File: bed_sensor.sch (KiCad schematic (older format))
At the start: 13 parts, among them J1 Conn_01x02, J2 Conn_01x06, J3 Conn_01x02, J4 Conn_01x08, Q1 2N2219, SW1 SW_SPST

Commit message: add csv
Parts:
- RV1: footprint Potentiometer_THT:Potentiometer_ACP_CA6-H2,5_Horizontal -> Potentiometer_THT:Potentiometer_Piher_PC-16_Single_Vertical
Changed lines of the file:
@@
 EESchema Schematic File Version 4
+LIBS:bed_sensor-cache
 EELAYER 26 0
 EELAYER END
@@
 F 0 "RV1" H 4530 3604 50  0000 R CNN
 F 1 "10K" H 4530 3695 50  0000 R CNN
-F 2 "Potentiometer_THT:Potentiometer_ACP_CA6-H2,5_Horizontal" H 4600 3650 50  0001 C CNN
+F 2 "Potentiometer_THT:Potentiometer_Piher_PC-16_Single_Vertical" H 4600 3650 50  0001 C CNN
 F 3 "~" H 4600 3650 50  0001 C CNN
 	1    4600 3650

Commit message: added CFAH0802d
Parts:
- removed BZ1: Buzzer, Buzzer_Beeper:MagneticBuzzer_Kingstate_KCG0601, symbol Device:Buzzer
- removed D1: D, Diode_THT:D_DO-35_SOD27_P7.62mm_Horizontal, symbol Device:D
- removed DS1: WC1602A, components:NHD-0216HZ-FSW-FBW-33V3C, symbol Display_Character:WC1602A
- removed J1: Conn_01x02, components:JSTPH2, symbol Connector_Generic:Conn_01x02
- removed J2: Conn_01x06, Connector_PinHeader_2.54mm:PinHeader_1x06_P2.54mm_Horizontal, symbol Connector_Generic:Conn_01x06
- removed J3: Conn_01x02, Connector_PinHeader_2.54mm:PinHeader_1x02_P2.54mm_Vertical, symbol Connector_Generic:Conn_01x02
- removed J4: Conn_01x08, Connector_PinSocket_2.54mm:PinSocket_1x08_P2.54mm_Vertical, symbol Connector_Generic:Conn_01x08
- removed Q1: 2N2219, Package_TO_SOT_THT:TO-92_Inline, symbol Transistor_BJT:2N2219
- removed R1: 220, Resistor_THT:R_Axial_DIN0207_L6.3mm_D2.5mm_P7.62mm_Horizontal, symbol Device:R
- removed R2: 1K, Resistor_THT:R_Axial_DIN0207_L6.3mm_D2.5mm_P7.62mm_Horizontal, symbol Device:R
- removed RV1: 10K, Potentiometer_THT:Potentiometer_Piher_PC-16_Single_Vertical, symbol Device:POT
- removed SW1: SW_SPST, Button_Switch_THT:SW_CuK_OS102011MA1QN1_SPDT_Angled, symbol Switch:SW_SPST
- removed uP1: ARDUPROMINI, components:ArduProMini, symbol ardunio_mini:ARDUPROMINI
- added BZ?: Buzzer, symbol Device:Buzzer
- added C? (x2): CP1, symbol Device:CP1
- added C?: C, symbol Device:C
- added D?: LED, symbol Device:LED
- added D?: D, symbol Device:D
- added J?: Conn_01x02, symbol Connector:Conn_01x02
- added Q?: 2N2219, Package_TO_SOT_THT:TO-39-3, symbol Transistor_BJT:2N2219
- added R? (x2): R, symbol Device:R
- added R?: 220, symbol Device:R
- added RV?: POT, symbol device:POT
- added SW?: SW_DPST_x2, symbol foot_sensor-rescue:SW_DPST_x2
- added U?: CFAH0802D-YYH-JP, symbol Crystalfontz:CFAH0802D-YYH-JP
- added U?: SPX3819M5-L-3-3, TO_SOT_Packages_SMD:SOT-23-5, symbol foot_sensor-rescue:SPX3819M5-L-3-3
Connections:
- net labels added: Buzzer, Display_Enable, Vibration
- net labels removed: E, SCL, SDA, buzzer, vib
- wire segments 3 -> 20

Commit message: updated schematic
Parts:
- removed J?: Conn_01x02, symbol Connector:Conn_01x02
- removed RV?: POT, symbol device:POT
- removed SW?: SW_DPST_x2, symbol foot_sensor-rescue:SW_DPST_x2
- removed U?: CFAH0802D-YYH-JP, symbol Crystalfontz:CFAH0802D-YYH-JP
- removed U?: SPX3819M5-L-3-3, TO_SOT_Packages_SMD:SOT-23-5, symbol foot_sensor-rescue:SPX3819M5-L-3-3
- added C2: 10nF, Capacitor_SMD:C_0603_1608Metric, symbol Device:C
- added C5: .1uF, Capacitor_SMD:C_0603_1608Metric, symbol Device:C
- added C6: 1uF, Capacitor_SMD:C_0603_1608Metric, symbol Device:C
- added C7: 10uF, Capacitor_SMD:C_0603_1608Metric, symbol Device:C
- added J1: Conn_01x02, Connector_PinHeader_2.54mm:PinHeader_1x02_P2.54mm_Vertical, symbol Connector_Generic:Conn_01x02
- added J?: Conn_01x02, symbol Connector_Generic:Conn_01x02
- added L1: 10uH, Inductors_SMD:L_Taiyo-Yuden_NR-40xx, symbol Device:L_Core_Ferrite_Small
- added Q2, Q3: BSS138, Package_TO_SOT_SMD:SOT-23, symbol Transistor_FET:BSS138
- added R1, R2, R6, R7: 10k, Resistor_SMD:R_0805_2012Metric, symbol Device:R
- added RV1: 10K, Potentiometers:Potentiometer_Trimmer_ACP_CA9h2.5_Vertical_Px2.5mm_Py5.0mm, symbol Device:R_POT
- added SW1: SW_SPST, components:SW_CuK_OS102011MA1QN1_SPDT_Angled, symbol Switch:SW_SPST
- added U1: MIC5205-3.3, Package_TO_SOT_SMD:SOT-23-5, symbol Regulator_Linear:MIC5205-3.3
- added U2: MPU-9250, Package_DFN_QFN:QFN-24-1EP_3x3mm_P0.4mm_EP1.75x1.6mm, symbol Sensor_Motion:MPU-9250
- added U3: TXB0104D, Package_SO:SOIC-14_3.9x8.7mm_P1.27mm, symbol Logic_LevelTranslator:TXB0104D
- added U4: LTC3525-5, Package_TO_SOT_SMD:SOT-363_SC-70-6, symbol Regulator_Switching:LTC3525-5
- added U5: CFAH0802D-YYH-JP, components:CFAH0802D-YYH-JP, symbol Crystalfontz:CFAH0802D-YYH-JP
- BZ1: renamed from BZ?; footprint (none) -> components:PS1240P02BT
- C1: renamed from C?; value CP1 -> 10uF; footprint (none) -> Capacitors_Tantalum_SMD:CP_Tantalum_Case-T_EIA-3528-12_Reflow
- C3: renamed from C?; value CP1 -> 10uF; footprint (none) -> Capacitors_Tantalum_SMD:CP_Tantalum_Case-B_EIA-3528-21_Reflow
- C4: renamed from C?; value C -> .1uF; footprint (none) -> Capacitor_SMD:C_0603_1608Metric
- D1: renamed from D?; footprint (none) -> LED_SMD:LED_0603_1608Metric
- D2: renamed from D?; footprint (none) -> Diode_SMD:D_0603_1608Metric
- Q1: renamed from Q?; footprint Package_TO_SOT_THT:TO-39-3 -> Package_TO_SOT_SMD:SOT-723
- R3: renamed from R?; value R -> 10k; footprint (none) -> Resistor_SMD:R_0805_2012Metric
- R4: renamed from R?; value R -> 1K; footprint (none) -> Resistor_SMD:R_0805_2012Metric
- R5: renamed from R?; footprint (none) -> Resistor_SMD:R_0805_2012Metric
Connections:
- net labels added: +5V, SCL_MPU, SDA_MPU
- wire segments 20 -> 53
- no-connect marks 0 -> 2
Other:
- moved on the sheet: BZ1, D2, Q1, R4, R5

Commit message: updated design
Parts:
- J4: renamed from J?; footprint (none) -> components:JSTPH2
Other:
- moved on the sheet: BZ1, C2, C5, D2, J1, J4, Q1, R1, R2, R4, U2

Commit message: updated design
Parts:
- removed C6: 1uF, Capacitor_SMD:C_0603_1608Metric, symbol Device:C
- removed C7: 10uF, Capacitor_SMD:C_0603_1608Metric, symbol Device:C
- removed L1: 10uH, Inductors_SMD:L_Taiyo-Yuden_NR-40xx, symbol Device:L_Core_Ferrite_Small
- removed Q2, Q3: BSS138, Package_TO_SOT_SMD:SOT-23, symbol Transistor_FET:BSS138
- removed R6, R7: 10k, Resistor_SMD:R_0805_2012Metric, symbol Device:R
- removed U3: TXB0104D, Package_SO:SOIC-14_3.9x8.7mm_P1.27mm, symbol Logic_LevelTranslator:TXB0104D
- removed U4: LTC3525-5, Package_TO_SOT_SMD:SOT-363_SC-70-6, symbol Regulator_Switching:LTC3525-5
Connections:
- net +5V is gone; now on net +3V3: R5.1, RV1.1, U5.2 (Vdd)
- net DB4: now also U5.11 (DB4)
- net DB5: now also U5.12 (DB5)
- net DB6: now also U5.13 (DB6)
- net DB7: now also U5.14 (DB7)
- net Display_Enable: now also U5.6 (E)
- net RS: now also U5.4 (RS)
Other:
- moved on the sheet: R5, RV1, U5

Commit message: updated pcb layout
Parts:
- added C6: .1uF, Capacitor_SMD:C_0603_1608Metric, symbol Device:C
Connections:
- net +3V3: now also C6.2
- net GND: now also C6.1
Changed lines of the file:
@@
 L power:+3.3V #PWR0134
 U 1 1 5B151EBC
-P 2950 4150
-F 0 "#PWR0134" H 2950 4000 50  0001 C CNN
-F 1 "+3.3V" H 2965 4323 50  0000 C CNN
-F 2 "" H 2950 4150 50  0001 C CNN
-F 3 "" H 2950 4150 50  0001 C CNN
-	1    2950 4150
+P 2950 3950
+F 0 "#PWR0134" H 2950 3800 50  0001 C CNN
+F 1 "+3.3V" H 2965 4123 50  0000 C CNN
+F 2 "" H 2950 3950 50  0001 C CNN
+F 3 "" H 2950 3950 50  0001 C CNN
+	1    2950 3950
 	1    0    0    -1
 $EndComp
@@
 	0    -1   -1   0
 $EndComp
+$Comp
+L Device:C C6
+U 1 1 5B20EB30
+P 3100 4050
+F 0 "C6" V 2848 4050 50  0000 C CNN
+F 1 ".1uF" V 2939 4050 50  0000 C CNN
+F 2 "Capacitor_SMD:C_0603_1608Metric" H 3138 3900 50  0001 C CNN
+F 3 "~" H 3100 4050 50  0001 C CNN
+	1    3100 4050
+	0    1    1    0
+$EndComp
+$Comp
+L power:GND #PWR0119
+U 1 1 5B20EC20
+P 3250 4050
+F 0 "#PWR0119" H 3250 3800 50  0001 C CNN
+F 1 "GND" V 3255 3922 50  0000 R CNN
+F 2 "" H 3250 4050 50  0001 C CNN
+F 3 "" H 3250 4050 50  0001 C CNN
+	1    3250 4050
+	0    -1   -1   0
+$EndComp
+Wire Wire Line
+	2950 4150 2950 4050
+Connection ~ 2950 4050
+Wire Wire Line
+	2950 4050 2950 3950
 $EndSCHEMATC

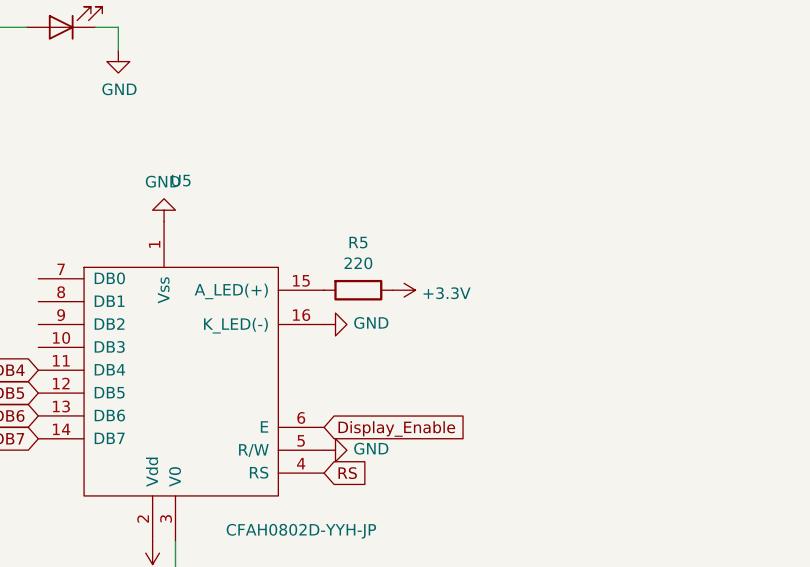
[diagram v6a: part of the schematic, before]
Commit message: corrected pinout for NHD display
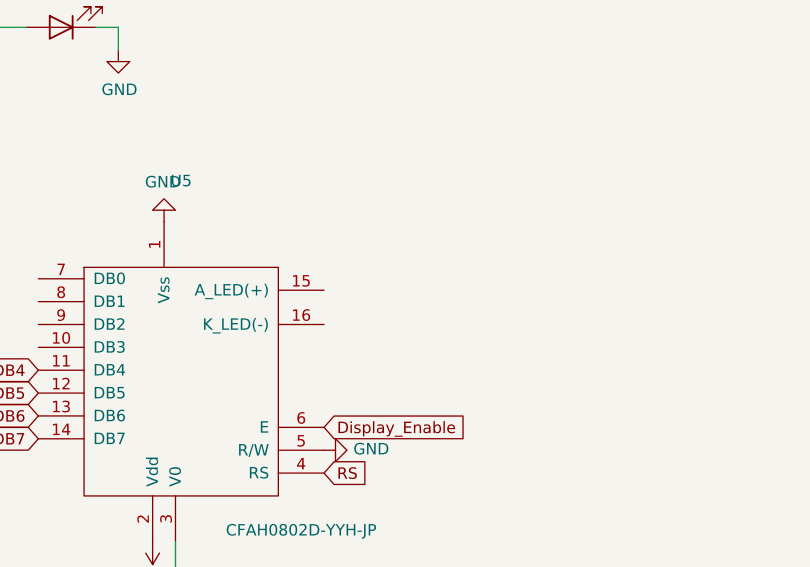
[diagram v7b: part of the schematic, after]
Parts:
- removed R5: 220, Resistor_SMD:R_0805_2012Metric, symbol Device:R
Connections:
- net GND: no longer U5.16 (K_LED(-))
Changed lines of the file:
@@
 Text GLabel 5350 5000 2    50   Input ~ 0
 DB5
-$Comp
-L Device:R R5
-U 1 1 5B1151FC
-P 5650 2300
-F 0 "R5" V 5443 2300 50  0000 C CNN
-F 1 "220" V 5534 2300 50  0000 C CNN
-F 2 "Resistor_SMD:R_0805_2012Metric" V 5580 2300 50  0001 C CNN
-F 3 "~" H 5650 2300 50  0001 C CNN
-	1    5650 2300
-	0    1    1    0
-$EndComp
 Text GLabel 5350 5100 2    50   Input ~ 0
 Vibration
@@
 	1    0    0    -1
 $EndComp
-$Comp
-L power:GND #PWR0117
-U 1 1 5B11EDA1
-P 5500 2450
-F 0 "#PWR0117" H 5500 2200 50  0001 C CNN
-F 1 "GND" V 5505 2322 50  0000 R CNN
-F 2 "" H 5500 2450 50  0001 C CNN
-F 3 "" H 5500 2450 50  0001 C CNN
-	1    5500 2450
-	0    -1   -1   0
-$EndComp
 Wire Wire Line
 	4850 3400 4850 3700
@@
 $EndComp
 $Comp
-L power:+3.3V #PWR0116
-U 1 1 5B20C130
-P 5800 2300
-F 0 "#PWR0116" H 5800 2150 50  0001 C CNN
-F 1 "+3.3V" V 5815 2428 50  0000 L CNN
-F 2 "" H 5800 2300 50  0001 C CNN
-F 3 "" H 5800 2300 50  0001 C CNN
-	1    5800 2300
-	0    1    1    0
-$EndComp
-$Comp

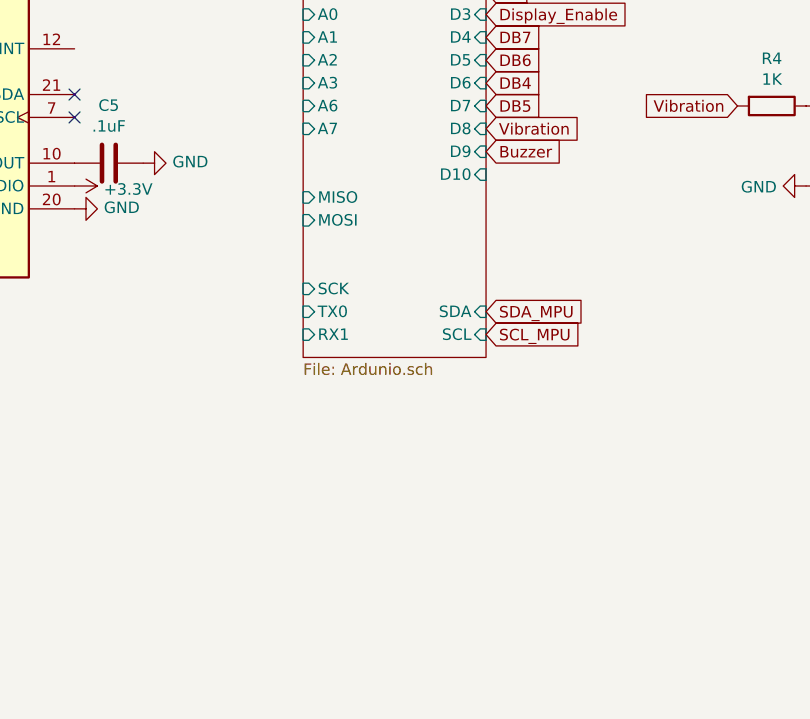
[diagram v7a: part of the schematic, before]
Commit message: added SD card
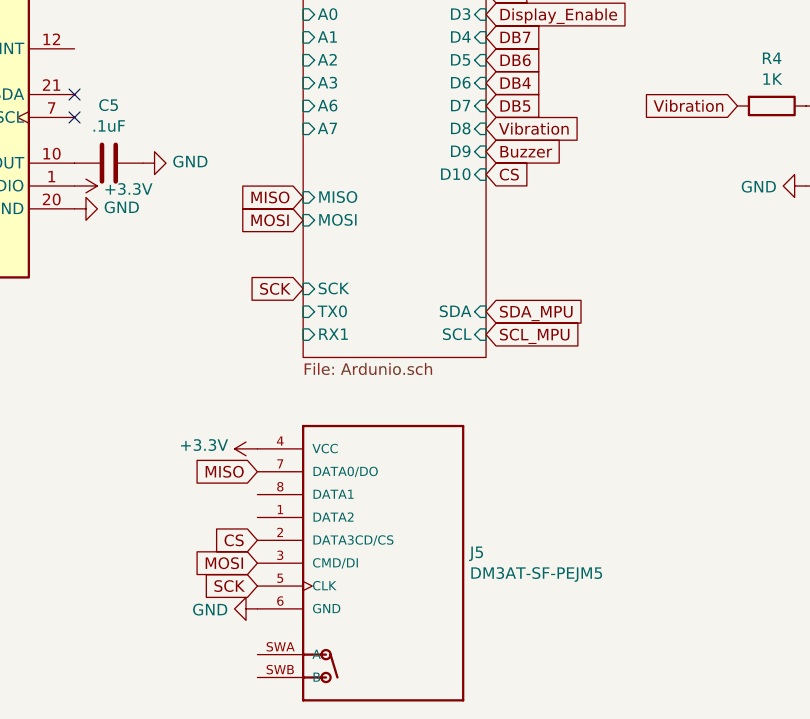
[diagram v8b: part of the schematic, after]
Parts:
- added J5: DM3AT-SF-PEJM5, components:HRS_DM3AT-SF-PEJM5, symbol SD:DM3AT-SF-PEJM5
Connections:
- net +3V3: now also J5.4 (VCC)
- net GND: now also J5.6 (GND)
- new net CS: J5.2 (DATA3CD/CS)
- new net MISO: J5.7 (DATA0/DO)
- new net MOSI: J5.3 (CMD/DI)
- new net SCK: J5.5 (CLK)
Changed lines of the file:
@@
 Wire Wire Line
 	2950 4050 2950 3950
+$Comp
+L SD:DM3AT-SF-PEJM5 J5
+U 1 1 5B292A17
+P 4550 7000
+F 0 "J5" H 5279 7046 50  0000 L CNN
+F 1 "DM3AT-SF-PEJM5" H 5279 6955 50  0000 L CNN
+F 2 "components:HRS_DM3AT-SF-PEJM5" H 4550 7000 50  0001 L BNN
+F 3 "None" H 4550 7000 50  0001 L BNN
+F 4 "Hirose" H 4550 7000 50  0001 L BNN "Field4"
+F 5 "DM3AT-SF-PEJM5" H 4550 7000 50  0001 L BNN "Field5"
+F 6 "Warning" H 4550 7000 50  0001 L BNN "Field6"
+F 7 "2.58 USD" H 4550 7000 50  0001 L BNN "Field7"
+F 8 "DM3 RA SMT microSD memory card push/push" H 4550 7000 50  0001 L BNN "Field8"
+	1    4550 7000
+	1    0    0    -1
+$EndComp
+$Comp
+L power:+3.3V #PWR0116
+U 1 1 5B292D16
+P 4350 6500
+F 0 "#PWR0116" H 4350 6350 50  0001 C CNN
+F 1 "+3.3V" V 4365 6628 50  0000 L CNN
+F 2 "" H 4350 6500 50  0001 C CNN
+F 3 "" H 4350 6500 50  0001 C CNN
+	1    4350 6500
+	0    -1   -1   0
+$EndComp
+Text GLabel 4350 6900 0    50   Input ~ 0
+CS
+Text GLabel 5350 5300 2    50   Input ~ 0
+CS
+Text GLabel 4350 7100 0    50   Input ~ 0
+SCK
+Text GLabel 4550 5800 0    50   Input ~ 0
+SCK
+$Comp
+L power:GND #PWR?
+U 1 1 5B293C50
+P 4350 7200
+F 0 "#PWR?" H 4350 6950 50  0001 C CNN
+F 1 "GND" V 4355 7072 50  0000 R CNN
+F 2 "" H 4350 7200 50  0001 C CNN
+F 3 "" H 4350 7200 50  0001 C CNN
+	1    4350 7200
+	0    1    1    0
+$EndComp
+Text GLabel 4550 5500 0    50   Input ~ 0
+MOSI
+Text GLabel 4350 7000 0    50   Input ~ 0
+MOSI
+Text GLabel 4550 5400 0    50   Input ~ 0
+MISO
+Text GLabel 4350 6600 0    50   Input ~ 0
+MISO
 $EndSCHEMATC
